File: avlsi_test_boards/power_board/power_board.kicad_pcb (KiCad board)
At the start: 4 copper layers, 116 parts, among them J1 PJ-102AH, J2 PJ-102AH, J3 Conn_02x06_Top_Bottom, J4 Conn_02x06_Top_Bottom, J5 Conn_02x20_Odd_Even, J6 Conn_02x20_Odd_Even, J7 Conn_02x20_Odd_Even, J8 Conn_02x20_Odd_Even, U1 TLV1117LV18DCYR, U11 SN74LVC16T245DLR, U12 SN74LVC16T245DLR, U13 SN74LVC16T245DLR, U14 SN74LVC16T245DLR, U15 DS04-254-2-04BK-SMT, U17 SN74LVC16T245DLR, U18 SN74LVC16T245DLR, U19 SN74LVC16T245DLR, U20 74HC4051D_653, U3 TLV1117LV25DCYR, U4 TLV1117LV33DCYR, U5 TLV1117LV18DCYR, U6 TLV75709PDBV, U7 TLV1117LV25DCYR, U8 TLV1117LV33DCYR

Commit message: Fully routed
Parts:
- removed the C1 at (90.5, 48.5)
- removed the C1 at (81.5, 27.0)
- removed the C1 at (72.0, 49.8)
- removed the C10 at (43.0, 66.3)
- removed the C12 at (31.8, 41.5)
- removed the C17 at (81.5, 34.5)
- removed the C17 at (90.5, 53.5)
- removed the C17 at (43.5, 56.2)
- removed the C18 at (81.5, 37.0)
- removed the C18 at (90.5, 56.0)
- removed the C18 at (78.5, 62.5)
- removed the C2 at (81.5, 29.5)
- removed the C2 at (90.5, 51.0)
- removed the C2 at (35.5, 49.0)
- removed the C38 at (51.0, 78.9)
- removed the C38 at (23.5, 51.2)
- removed the C39 at (55.0, 63.8)
- removed the C39 at (23.5, 53.7)
- removed the C6 at (52.1, 55.0)
- removed the C6 at (51.9, 41.5)
- removed the C7 at (81.5, 32.0)
- removed the C7 at (61.0, 63.8)
- removed the C9 at (43.0, 63.8)
- removed J4: Conn_02x06_Top_Bottom, Connector_PinHeader_2.54mm:PinHeader_2x06_P2.54mm_Vertical
- added C1: 1u, Capacitor_SMD:C_0603_1608Metric, B.Cu at (151.9, 58.8)
- added C17: 1u, Capacitor_SMD:C_0603_1608Metric, B.Cu at (169.6, 46.3)
- added C18: 1u, Capacitor_SMD:C_0603_1608Metric, B.Cu at (169.5, 59.0)
- added C2: 1u, Capacitor_SMD:C_0603_1608Metric, B.Cu at (151.8, 53.8)
- added C38: 1u, Capacitor_SMD:C_0603_1608Metric, B.Cu at (156.6, 101.9)
- added C39: 1u, Capacitor_SMD:C_0603_1608Metric, B.Cu at (121.6, 103.5)
- added C6: 1u, Capacitor_SMD:C_0603_1608Metric, B.Cu at (109.3, 103.4)
- added C7: 1u, Capacitor_SMD:C_0603_1608Metric, B.Cu at (179.0, 52.3)
- added J9: Conn_02x07_Top_Bottom, Connector_PinHeader_2.00mm:PinHeader_2x07_P2.00mm_Vertical, F.Cu at (188.7, 35.8)
- added REF**: MountingHole_3.7mm, MountingHole:MountingHole_3.7mm, F.Cu at (195.4, 36.4)
- added REF**: MountingHole_3.7mm, MountingHole:MountingHole_3.7mm, F.Cu at (195.4, 128.2)
- added REF**: MountingHole_3.7mm, MountingHole:MountingHole_3.7mm, F.Cu at (103.6, 36.4)
- added REF**: MountingHole_3.7mm, MountingHole:MountingHole_3.7mm, F.Cu at (103.6, 128.1)
- C11, C12, C13, C15, C16, C19, C20, C22, C23, C24, C25, C26, C27, C28, C29, C30, C31, C32, C33, C34, C35, C36, C37, C4, C40, C41, C42, C43, C44, C47, C48, C51, C52: moved to B.Cu
- J3: value Conn_02x06_Top_Bottom -> Conn_02x07_Top_Bottom; footprint Connector_PinHeader_2.54mm:PinHeader_2x06_P2.54mm_Vertical -> Connector_PinHeader_2.00mm:PinHeader_2x07_P2.00mm_Vertical
- S5: moved to F.Cu
- moved C5 161.4 mm to (187.9, 46.4), turned to 90 degrees
- moved C20 147.2 mm to (190.1, 103.1), turned to 90 degrees
- moved C28 146.2 mm to (190.1, 111.1), turned to -90 degrees
- moved R11 145.0 mm to (190.4, 87.4), turned to 90 degrees
- moved R5 144.7 mm to (190.5, 79.1), turned to 90 degrees
- moved C44 142.2 mm to (190.1, 118.2), turned to -90 degrees
- moved C30 141.0 mm to (190.1, 94.3), turned to -90 degrees
- moved C13 137.5 mm to (177.7, 101.4), turned to -90 degrees
- moved C12 137.0 mm to (177.7, 96.2), turned to 90 degrees
- moved C29 133.6 mm to (177.7, 111.2), turned to -90 degrees
- moved C43 132.0 mm to (177.7, 120.0), turned to 90 degrees
- moved C10 131.1 mm to (156.5, 71.6), turned to -90 degrees
- moved R13 127.3 mm to (175.0, 79.3), turned to 90 degrees
- moved C45 127.3 mm to (143.9, 71.7), turned to -90 degrees
- moved R1 122.8 mm to (174.8, 70.9), turned to -90 degrees
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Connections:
- C10 pad 1: /pin_header/GND -> DGND
- C11 pad 1: /pin_header/GND -> DGND
- C12 pad 1: /pin_header/GND -> DGND
- C13 pad 1: /pin_header/GND -> DGND
- C14 pad 1: /pin_header/GND -> DGND
- C15 pad 1: /pin_header/GND -> DGND
- C16 pad 1: /pin_header/GND -> DGND
- C19 pad 1: /pin_header/GND -> DGND
- C20 pad 1: /pin_header/GND -> DGND
- C21 pad 2: /digital_power_converters/GND -> DGND
- C22 pad 2: /digital_power_converters/GND -> DGND
- C23 pad 1: /pin_header/GND -> DGND
- C24 pad 1: /pin_header/GND -> DGND
- C25 pad 1: /pin_header/GND -> DGND
- C26 pad 1: /pin_header/GND -> DGND
- C27 pad 1: /pin_header/GND -> DGND
- C28 pad 1: /pin_header/GND -> DGND
- C29 pad 1: /pin_header/GND -> DGND
- C3 pad 2: /digital_power_converters/GND -> DGND
- C30 pad 1: /pin_header/GND -> DGND
- C31 pad 1: /AVIN -> /AVIN5
- C31 pad 2: /AGND -> ADGND
- C32 pad 1: /AVIN -> /AVIN5
- C32 pad 2: /AGND -> ADGND
- C33 pad 2: /AGND -> ADGND
- C34 pad 2: /AGND -> ADGND
- C35 pad 1: /pin_header/GND -> DGND
- C36 pad 1: /pin_header/GND -> DGND
- C37 pad 1: /AVIN -> /AVIN5
- C37 pad 2: /AGND -> ADGND
- C4 pad 2: /digital_power_converters/GND -> DGND
- C40 pad 1: /pin_header/GND -> DGND
- C41 pad 1: /pin_header/GND -> DGND
- C42 pad 2: /AGND -> ADGND
- C43 pad 1: /pin_header/GND -> DGND
- C44 pad 1: /pin_header/GND -> DGND
- C45 pad 1: /pin_header/GND -> DGND
- C47 pad 1: /AVIN -> /AVIN5
- C47 pad 2: /AGND -> ADGND
- C48 pad 1: /AVIN -> /AVIN5
- C48 pad 2: /AGND -> ADGND
- C5 pad 1: /digital_power_converters/GND -> DGND
- C5 pad 2: /digital_power_converters/VIN -> DVIN5
- C51 pad 2: /AGND -> ADGND
- C52 pad 2: /AGND -> ADGND
- C8 pad 2: /digital_power_converters/GND -> DGND
- C9 pad 1: /pin_header/GND -> DGND
- J1 pad 1: /DVIN -> DVIN5
- J1 pad 2: /DGND -> DGND
- J1 pad 3: /DGND -> DGND
- J2 pad 1: /AVIN -> /AVIN5
- J2 pad 2: /AGND -> ADGND
- J2 pad 3: /AGND -> ADGND
- J3 pad 1: /DVIN -> ADGND
- J3 pad 10: /DGND -> /VCCA12
- J3 pad 11: /VCCD12 -> ADGND
- J3 pad 12: /DGND -> /VCCA09
- J3 pad 2: /DGND -> /AVIN5
- J3 pad 3: /VCCD18 -> ADGND
- J3 pad 4: /DGND -> /VCCA33
- J3 pad 5: /VCCD09 -> ADGND
- J3 pad 6: /DGND -> /VCCA25
- J3 pad 7: /VCCD33 -> ADGND
- J3 pad 8: /DGND -> /VCCA18
- J3 pad 9: /VCCD25 -> ADGND
- J5 pad 1: /pin_header/DGND -> DGND
- J5 pad 10: /pin_header/DGND -> DGND
- J5 pad 16: /pin_header/DGND -> DGND
- J5 pad 19: /pin_header/DGND -> DGND
- J5 pad 2: /pin_header/DGND -> DGND
- J5 pad 20: /pin_header/DGND -> DGND
- J5 pad 21: /pin_header/HA15 -> /pin_header/HA16
- J5 pad 22: /pin_header/HA16 -> /pin_header/HA15
- J5 pad 23: /pin_header/HA13 -> /pin_header/HA14
- J5 pad 24: /pin_header/HA14 -> /pin_header/HA13
- J5 pad 25: /pin_header/HA11 -> /pin_header/HA12
- J5 pad 26: /pin_header/HA12 -> /pin_header/HA11
- J5 pad 27: /pin_header/HA9 -> /pin_header/HA10
- J5 pad 28: /pin_header/HA10 -> /pin_header/HA9
- J5 pad 29: /pin_header/HA7 -> /pin_header/HA8
- J5 pad 30: /pin_header/HA8 -> /pin_header/HA7
- J5 pad 31: /pin_header/HA5 -> /pin_header/HA6
- J5 pad 32: /pin_header/HA6 -> /pin_header/HA5
- J5 pad 33: /pin_header/HA3 -> /pin_header/HA4
- J5 pad 34: /pin_header/HA4 -> /pin_header/HA3
- J5 pad 35: /pin_header/HA1 -> /pin_header/HA2
- J5 pad 36: /pin_header/HA2 -> /pin_header/HA1
- J5 pad 37: /pin_header/OPF1 -> /pin_header/OPH1
- J5 pad 38: /pin_header/OPH1 -> /pin_header/OPF1
- J5 pad 39: /pin_header/OPH2 -> /pin_header/OPH3
- J5 pad 40: /pin_header/OPH3 -> /pin_header/OPH2
- J6 pad 1: /pin_header/HB7 -> /pin_header/HB8
- J6 pad 2: /pin_header/HB8 -> /pin_header/HB7
- J6 pad 3: /pin_header/HB5 -> /pin_header/HB6
- J6 pad 4: /pin_header/HB6 -> /pin_header/HB5
- J6 pad 5: /pin_header/HB3 -> /pin_header/HB4
- J6 pad 6: /pin_header/HB4 -> /pin_header/HB3
- J6 pad 7: /pin_header/HB1 -> /pin_header/HB2
- J6 pad 8: /pin_header/HB2 -> /pin_header/HB1
- J7 pad 21: /pin_header/DGND -> DGND
- J7 pad 22: /pin_header/DGND -> DGND
- J7 pad 23: /pin_header/DGND -> DGND
- J7 pad 24: /pin_header/DGND -> DGND
- J7 pad 26: /pin_header/DGND -> DGND
- J7 pad 29: /pin_header/DGND -> DGND
- J7 pad 35: /pin_header/DGND -> DGND
- J8 pad 3: /pin_header/HB11 -> /pin_header/HB12
- J8 pad 4: /pin_header/HB12 -> /pin_header/HB11
- J8 pad 5: /pin_header/HB13 -> /pin_header/HB14
- J8 pad 6: /pin_header/HB14 -> /pin_header/HB13
- J8 pad 7: /pin_header/HB15 -> /pin_header/HB16
- J8 pad 8: /pin_header/HB16 -> /pin_header/HB15
- R1 pad 2: /pin_header/GND -> DGND
- R10 pad 2: /pin_header/GND -> DGND
- R11 pad 2: /pin_header/GND -> DGND
- R12 pad 2: /pin_header/GND -> DGND
- R13 pad 2: /pin_header/GND -> DGND
- R14 pad 2: /pin_header/GND -> DGND
- R15 pad 1: /digital_power_converters/GND -> DGND
- R16 pad 1: /digital_power_converters/GND -> DGND
- R17 pad 1: /digital_power_converters/GND -> DGND
- R2 pad 2: /pin_header/GND -> DGND
- R3 pad 2: /pin_header/GND -> DGND
- R4 pad 1: unconnected-(R4-Pad1) -> /pin_header/DIR1_6
- R4 pad 2: /pin_header/GND -> DGND
- R5 pad 2: /pin_header/GND -> DGND
- R6 pad 2: /pin_header/GND -> DGND
- R7 pad 2: /pin_header/GND -> DGND
- R8 pad 2: /pin_header/GND -> DGND
- R9 pad 2: /pin_header/GND -> DGND
- S1 pad A2: /pin_header/VIN -> V_Level_Shift
- S1 pad B2: /pin_header/VIN -> V_Level_Shift
- S2 pad A2: /pin_header/VIN -> V_Level_Shift
- S2 pad B2: /pin_header/VIN -> V_Level_Shift
- S3 pad A2: /pin_header/VIN -> V_Level_Shift
- S3 pad B2: /pin_header/VIN -> V_Level_Shift
- S4 pad A2: /pin_header/VIN -> V_Level_Shift
- S4 pad B2: /pin_header/VIN -> V_Level_Shift
- S5 pad A2: /pin_header/VIN -> V_Level_Shift
- S5 pad B2: /pin_header/VIN -> V_Level_Shift
- S6 pad A2: /pin_header/VIN -> V_Level_Shift
- S6 pad B2: /pin_header/VIN -> V_Level_Shift
- S7 pad A2: /pin_header/VIN -> V_Level_Shift
- S7 pad B2: /pin_header/VIN -> V_Level_Shift
- U1 pad 1: /digital_power_converters/GND -> DGND
- U1 pad 3: /digital_power_converters/VIN -> DVIN5
- U11 pad 10: /pin_header/GND -> DGND
- U11 pad 15: /pin_header/GND -> DGND
- U11 pad 21: /pin_header/GND -> DGND
- U11 pad 28: /pin_header/GND -> DGND
- U11 pad 34: /pin_header/GND -> DGND
- U11 pad 39: /pin_header/GND -> DGND
- U11 pad 4: /pin_header/GND -> DGND
- U11 pad 45: /pin_header/GND -> DGND
- U12 pad 10: /pin_header/GND -> DGND
- U12 pad 15: /pin_header/GND -> DGND
- U12 pad 21: /pin_header/GND -> DGND
- U12 pad 28: /pin_header/GND -> DGND
- U12 pad 34: /pin_header/GND -> DGND
- U12 pad 39: /pin_header/GND -> DGND
- U12 pad 4: /pin_header/GND -> DGND
- U12 pad 45: /pin_header/GND -> DGND
- U13 pad 10: /pin_header/GND -> DGND
- U13 pad 15: /pin_header/GND -> DGND
- U13 pad 21: /pin_header/GND -> DGND
- U13 pad 28: /pin_header/GND -> DGND
- U13 pad 34: /pin_header/GND -> DGND
- U13 pad 39: /pin_header/GND -> DGND
- U13 pad 4: /pin_header/GND -> DGND
- U13 pad 45: /pin_header/GND -> DGND
- U14 pad 10: unconnected-(U14-GND-Pad10) -> DGND
- U14 pad 15: /pin_header/GND -> DGND
- U14 pad 21: /pin_header/GND -> DGND
- U14 pad 28: /pin_header/GND -> DGND
- U14 pad 34: /pin_header/GND -> DGND
- U14 pad 39: /pin_header/GND -> DGND
- U14 pad 4: /pin_header/GND -> DGND
- U14 pad 45: /pin_header/GND -> DGND
- U15 pad 1: /digital_power_converters/VIN -> DVIN5
- U15 pad 2: /digital_power_converters/VIN -> DVIN5
- U15 pad 3: /digital_power_converters/VIN -> DVIN5
- U15 pad 4: /digital_power_converters/VIN -> DVIN5
- U17 pad 10: unconnected-(U17-GND-Pad10) -> DGND
- U17 pad 15: /pin_header/GND -> DGND
- U17 pad 21: /pin_header/GND -> DGND
- U17 pad 28: /pin_header/GND -> DGND
- U17 pad 34: /pin_header/GND -> DGND
- U17 pad 39: /pin_header/HC6 -> DGND
- U17 pad 4: /pin_header/GND -> DGND
- U17 pad 40: /pin_header/GND -> /pin_header/HC6
- U17 pad 45: /pin_header/GND -> DGND
- U18 pad 10: /pin_header/GND -> DGND
- U18 pad 15: /pin_header/GND -> DGND
- U18 pad 21: /pin_header/GND -> DGND
- U18 pad 28: /pin_header/GND -> DGND
- U18 pad 34: /pin_header/GND -> DGND
- U18 pad 39: /pin_header/GND -> DGND
- U18 pad 4: /pin_header/GND -> DGND
- U18 pad 45: /pin_header/GND -> DGND
- U19 pad 10: /pin_header/GND -> DGND
- U19 pad 15: /pin_header/GND -> DGND
- U19 pad 21: /pin_header/GND -> DGND
- U19 pad 28: /pin_header/GND -> DGND
- U19 pad 34: /pin_header/GND -> DGND
- U19 pad 39: /pin_header/GND -> DGND
- U19 pad 4: /pin_header/GND -> DGND
- U19 pad 45: /pin_header/GND -> DGND
- U2 pad 02: /pin_header/DGND -> DGND
- U2 pad 116: /pin_header/DGND -> DGND
- U2 pad 136: /pin_header/DGND -> DGND
- U2 pad 14: /pin_header/DGND -> DGND
- U2 pad 158: /pin_header/DGND -> DGND
- U2 pad 160: /pin_header/DGND -> DGND
- U2 pad 35: /pin_header/DGND -> DGND
- U2 pad 55: /pin_header/DGND -> DGND
- U2 pad 78: /pin_header/DGND -> DGND
- U2 pad 80: /pin_header/DGND -> DGND
- U2 pad 81: /pin_header/DGND -> DGND
- U2 pad 93: /pin_header/DGND -> DGND
- U2 pad 94: /pin_header/DGND -> DGND
- U20 pad 16: /digital_power_converters/VIN -> DVIN5
- U20 pad 5: /digital_power_converters/AVIN -> VDCustom
- U20 pad 6: /digital_power_converters/VIN -> DVIN5
- U20 pad 7: /digital_power_converters/GND -> DGND
- U20 pad 8: /digital_power_converters/GND -> DGND
- U3 pad 1: /digital_power_converters/GND -> DGND
- U3 pad 3: /digital_power_converters/VIN -> DVIN5
- U4 pad 1: /digital_power_converters/GND -> DGND
- U4 pad 3: /digital_power_converters/VIN -> DVIN5
- U5 pad 1: /AGND -> ADGND
- U5 pad 3: /AVIN -> /AVIN5
- U6 pad 1: /AVIN -> /AVIN5
- U6 pad 2: /AGND -> ADGND
- U6 pad 3: /AVIN -> /AVIN5
- U7 pad 1: /AGND -> ADGND
- U7 pad 3: /AVIN -> /AVIN5
- U8 pad 1: /AGND -> ADGND
- U8 pad 3: /AVIN -> /AVIN5
- VR1 pad 1: /digital_power_converters/GND -> DGND
- VR1 pad 3: /digital_power_converters/VIN -> DVIN5
- VR2 pad 1: /AGND -> ADGND
- VR2 pad 3: /AVIN -> /AVIN5
- VR3 pad 1: /digital_power_converters/GND -> DGND
- VR3 pad 3: /digital_power_converters/VIN -> DVIN5
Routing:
- net DGND: track 0.00 -> 1122.4 mm, vias 0 -> 66
- net /pin_header/DGND: track 892.1 -> 0.00 mm
- net DVIN5: track 0.00 -> 127.1 mm, vias 0 -> 8
- net V_Level_Shift: track 392.2 -> 508.6 mm, vias 15 -> 54
- net /AVIN5: track 0.00 -> 98.0 mm, vias 0 -> 8
- net /pin_header/HB9: track 2.17 -> 71.2 mm
- net /AVIN: track 58.3 -> 0.00 mm, vias 1 -> 0
- net VDCustom: track 0.00 -> 49.6 mm, vias 0 -> 1
- net /pin_header/DIR2_0: track 93.4 -> 46.1 mm
- net /pin_header/DIR1_0: track 66.4 -> 25.2 mm, vias 4 -> 2
- net /VCCA25: track 52.5 -> 20.8 mm, vias 2 -> 1
- net /pin_header/DIR1_2: track 44.0 -> 19.2 mm, vias 2 -> 0
- net /VCCA18: track 39.9 -> 17.0 mm, vias 0 -> 1
- net /pin_header/DIR2_6: track 61.2 -> 38.8 mm, vias 4 -> 2
- net /pin_header/DIR1_4: track 46.3 -> 25.7 mm
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- added copper zone on B.Cu, net ADGND
- added copper zone on F.Cu, net ADGND
- added copper zone on B.Cu, net DGND
- added copper zone on F.Cu, net DGND
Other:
- board text added: "10VDD"
- board text added: "18VDD"
- board text added: "3VDD"
- board text added: "AGND"
- board text added: "AVIN5"
- board text added: "DGND"
- board text added: "Digital I/O"
- board text added: "FPGA_TCK"
- board text added: "FPGA_TDI"
- board text added: "FPGA_TDO"
- board text added: "FPGA_TMS"
- board text added: "Groudning pull up resistors near switches?"
- board text added: "Maybe the unfilled zone on the back is okay bevause its connected to ground through the back?"
- board text added: "NULL"
- board text added: "SYS_CLK_MC1"
- board text added: "SYS_CLK_MC2"
- board text added: "VACUSTOM"
- board text added: "VCCA09"
- board text added: "VCCA12"
- board text added: "VCCA18"
- board text added: "VCCA25"
- board text added: "VCCA33"
- board text added: "VCCBATT"
- board text added: "VCCO_MC1"
- board text added: "VCCO_MC2"
- board text added: "VDCIN"
- board text added: "XADC_VIN"
- board text added: "XADC_VP"

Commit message: more changes
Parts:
- removed J7: Conn_02x20_Odd_Even, Connector_PinHeader_2.00mm:PinHeader_2x20_P2.00mm_Vertical
- removed R4: 4.7k, Resistor_SMD:R_0201_0603Metric
- added J4: Conn_02x10_Odd_Even, Connector_PinHeader_2.00mm:PinHeader_2x10_P2.00mm_Vertical, F.Cu at (103.4, 63.1)
- moved C42 0.98 mm to (122.7, 55.5)
- moved U15 0.36 mm to (150.1, 38.5)
- moved R1 0.22 mm to (175.1, 70.9)
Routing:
- net DGND: track 1122.4 -> 1233.2 mm, vias 66 -> 123
- net /pin_header/VCCO_MC2: track 76.6 -> 87.7 mm
- net /pin_header/VCCO_MC1: track 120.8 -> 131.8 mm
- net DVIN5: track 127.1 -> 133.2 mm
- net /digital_power_converters/NULL: track 0.00 -> 5.35 mm
- net ADGND: track 12.2 -> 16.0 mm, vias 10 -> 11
- net /pin_header/VDCIN: track 161.9 -> 164.7 mm
- net /VCCA09: track 23.2 -> 25.1 mm
- net /pin_header/33VDD: track 194.9 -> 196.6 mm
- net /pin_header/3VDD: track 150.9 -> 152.5 mm
- net /pin_header/10VDD: track 95.9 -> 96.7 mm
- net /pin_header/HB8: track 45.4 -> 46.2 mm
- net /pin_header/SYS_CLK_MC2: track 27.8 -> 28.6 mm
- net /pin_header/HA2: track 40.8 -> 41.3 mm
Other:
- board outline added: 100 x 100 mm
- board text added: "LS1"
- board text added: "LS2"
- board text added: "LS3"
- board text added: "LS4"
- board text added: "LS5"
- board text added: "LS6"
- board text added: "LS7"
- board text added: "VA09"
- board text added: "VA12"
- board text added: "VA18"
- board text added: "VA27"
- board text added: "VA33"
- board text added: "VA50"
- board text added: "VCUST"
- board text added: "VD09"
- board text added: "VD12"
- board text added: "VD18"
- board text added: "VD27"
- board text added: "VD33"
- board text added: "VD50"
- board text removed: "10VDD"
- board text removed: "18VDD"
- board text removed: "3VDD"
- board text removed: "AVIN5"
- board text removed: "Digital I/O"
- board text removed: "FPGA_TCK"
- board text removed: "FPGA_TDI"
- board text removed: "FPGA_TDO"
- board text removed: "FPGA_TMS"
- board text removed: "NULL"
- board text removed: "SYS_CLK_MC1"
- board text removed: "SYS_CLK_MC2"
- board text removed: "VACUSTOM"
- board text removed: "VCCA09"
- board text removed: "VCCA12"
- board text removed: "VCCA18"
- board text removed: "VCCA25"
- board text removed: "VCCA33"
- board text removed: "VCCBATT"
- board text removed: "VCCO_MC1"
- board text removed: "VCCO_MC2"
- board text removed: "VDCIN"
- board text removed: "XADC_VIN"
- board text removed: "XADC_VP"

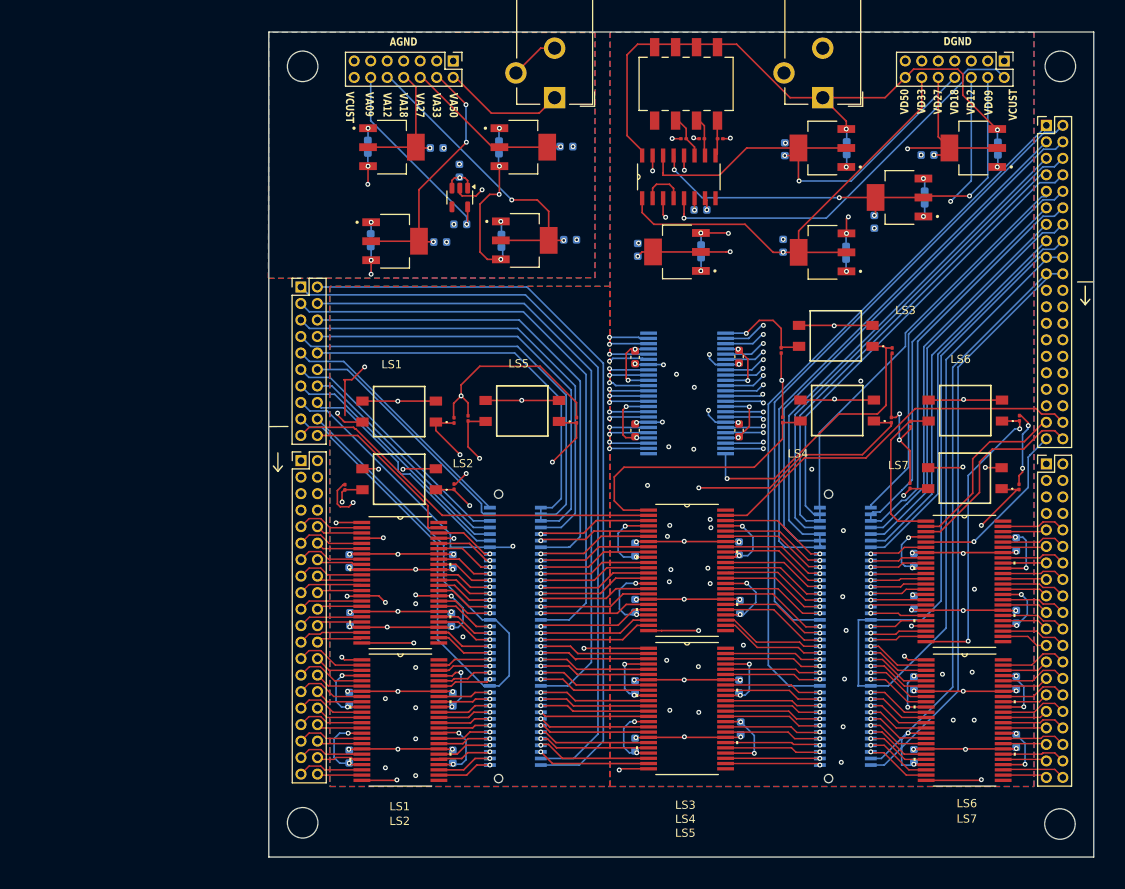
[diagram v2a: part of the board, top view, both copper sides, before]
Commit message: Add updated schematic
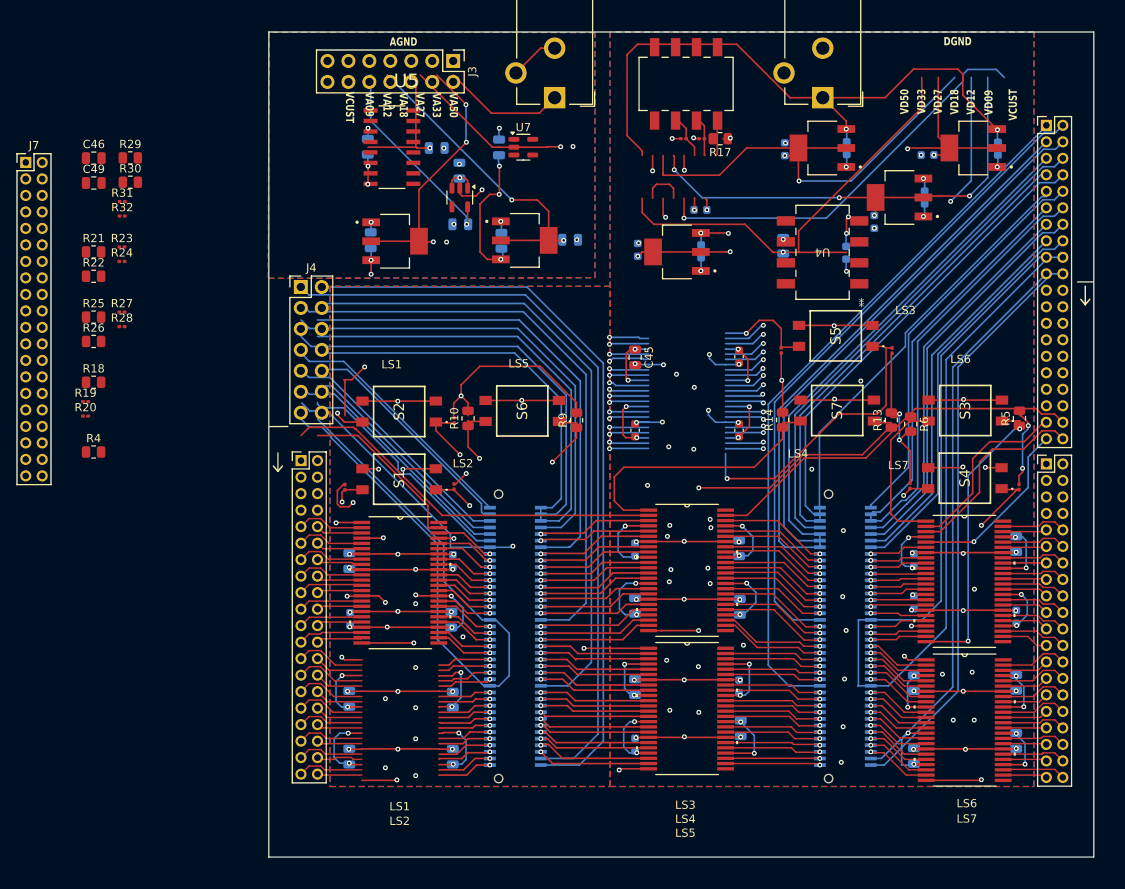
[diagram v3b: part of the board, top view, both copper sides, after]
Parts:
- removed C51, C52: 1u, Capacitor_SMD:C_0603_1608Metric
- removed J9: Conn_02x07_Top_Bottom, Connector_PinHeader_2.00mm:PinHeader_2x07_P2.00mm_Vertical
- removed REF** (x4): MountingHole_3.7mm, MountingHole:MountingHole_3.7mm
- removed U18, U19: SN74LVC16T245DLR, avlsi:DL48
- removed U20: 74HC4051D_653, 74HC4051D_653:SOIC127P600X175-16N
- added C46: 1u, Capacitor_SMD:C_0805_2012Metric, F.Cu at (78.3, 47.5)
- added C49: 0.1u, Capacitor_SMD:C_0805_2012Metric, F.Cu at (78.3, 50.5)
- added J7: Conn_02x20_Odd_Even, Connector_PinHeader_2.00mm:PinHeader_2x20_P2.00mm_Vertical, F.Cu at (70.0, 48.0)
- added R18: 10k, Resistor_SMD:R_0805_2012Metric, F.Cu at (78.3, 74.7)
- added R19: 4.7k, Resistor_SMD:R_0201_0603Metric, F.Cu at (77.3, 77.0)
- added R20: 4.7k, Resistor_SMD:R_0201_0603Metric, F.Cu at (77.3, 78.8)
- added R21: 10k, Resistor_SMD:R_0805_2012Metric, F.Cu at (78.3, 58.9)
- added R22: 10k, Resistor_SMD:R_0805_2012Metric, F.Cu at (78.3, 61.9)
- added R23: 4.7k, Resistor_SMD:R_0201_0603Metric, F.Cu at (81.7, 58.3)
- added R24: 4.7k, Resistor_SMD:R_0201_0603Metric, F.Cu at (81.7, 60.0)
- added R25: 10k, Resistor_SMD:R_0805_2012Metric, F.Cu at (78.3, 66.8)
- added R26: 10k, Resistor_SMD:R_0805_2012Metric, F.Cu at (78.3, 69.8)
- added R27: 4.7k, Resistor_SMD:R_0201_0603Metric, F.Cu at (81.7, 66.2)
- added R28: 4.7k, Resistor_SMD:R_0201_0603Metric, F.Cu at (81.7, 68.0)
- added R29: 10k, Resistor_SMD:R_0805_2012Metric, F.Cu at (82.7, 47.5)
- added R30: 10k, Resistor_SMD:R_0805_2012Metric, F.Cu at (82.7, 50.5)
- added R31: 4.7k, Resistor_SMD:R_0201_0603Metric, F.Cu at (81.7, 52.8)
- added R32: 4.7k, Resistor_SMD:R_0201_0603Metric, F.Cu at (81.7, 54.5)
- added R4: 0, Resistor_SMD:R_0805_2012Metric, F.Cu at (78.3, 83.2)
- C22, C24, C26, C28, C30, C32, C34, C36, C38, C40, C42, C44, C48: footprint Capacitor_SMD:C_0603_1608Metric -> Capacitor_SMD:C_0805_2012Metric
- C23, C25, C27, C29, C31, C33, C35, C37, C39, C41, C43, C45, C47: value 1u -> 0.1u; footprint Capacitor_SMD:C_0603_1608Metric -> Capacitor_SMD:C_0805_2012Metric
- J3: value Conn_02x07_Top_Bottom -> Conn_02x07_Odd_Even; footprint Connector_PinHeader_2.00mm:PinHeader_2x07_P2.00mm_Vertical -> Connector_PinHeader_2.54mm:PinHeader_2x07_P2.54mm_Vertical
- J4: value Conn_02x10_Odd_Even -> Conn_02x07_Odd_Even; footprint Connector_PinHeader_2.00mm:PinHeader_2x10_P2.00mm_Vertical -> Connector_PinHeader_2.54mm:PinHeader_2x07_P2.54mm_Vertical
- R10, R13, R14, R17, R5, R6, R9: value 4.7k -> 10k; footprint Resistor_SMD:R_0201_0603Metric -> Resistor_SMD:R_0805_2012Metric
- U4: value TLV1117LV33DCYR -> DS04-254-2-04BK-SMT; footprint avlsi:VREG_TLV1117LV33DCYR -> ds:DS04-254-2-04BK-SMT_CUD
- U5: value TLV1117LV18DCYR -> 74HC4051D_653; footprint avlsi:SOT230P700X180-4N -> 74HC4051D_653:SOIC127P600X175-16N
- U7: value TLV1117LV25DCYR -> TLV75709PDBV; footprint avlsi:SOT230P700X180-4N -> Package_TO_SOT_SMD:SOT-23-5
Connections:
- C10 pad 1: DGND -> VCCD12
- C10 pad 2: V_Level_Shift -> DGND
- C11 pad 2: V_Level_Shift -> DVIN5
- C12 pad 1: DGND -> /AVIN5
- C12 pad 2: V_Level_Shift -> ADGND
- C13 pad 1: DGND -> /AVIN5
- C13 pad 2: V_Level_Shift -> ADGND
- C14 pad 1: DGND -> /VCCA18
- C14 pad 2: V_Level_Shift -> ADGND
- C15 pad 1: DGND -> /VCCA12
- C15 pad 2: V_Level_Shift -> ADGND
- C16 pad 1: DGND -> /AVIN5
- C16 pad 2: V_Level_Shift -> ADGND
- C17 pad 1: DVIN5 -> /VCCA09
- C17 pad 2: DGND -> ADGND
- C18 pad 1: DVIN5 -> /AVIN5
- C18 pad 2: DGND -> ADGND
- C19 pad 1: DGND -> /AVIN5
- C19 pad 2: V_Level_Shift -> ADGND
- C20 pad 1: DGND -> /VCCA25
- C20 pad 2: V_Level_Shift -> ADGND
- C21 pad 1: /VCCD25 -> /VCCA33
- C21 pad 2: DGND -> ADGND
- C22 pad 1: /VCCD33 -> VCCD33
- C23 pad 1: DGND -> VCCD33
- C23 pad 2: V_Level_Shift -> DGND
- C24 pad 1: DGND -> V_Level_Shift
- C24 pad 2: V_Level_Shift -> DGND
- C25 pad 1: DGND -> V_Level_Shift
- C25 pad 2: V_Level_Shift -> DGND
- C26 pad 1: DGND -> VCCD33
- C26 pad 2: V_Level_Shift -> DGND
- C27 pad 1: DGND -> VCCD33
- C27 pad 2: V_Level_Shift -> DGND
- C28 pad 1: DGND -> V_Level_Shift
- C28 pad 2: V_Level_Shift -> DGND
- C29 pad 1: DGND -> V_Level_Shift
- C29 pad 2: V_Level_Shift -> DGND
- C3 pad 1: /VCCD18 -> DVIN5
- C30 pad 1: DGND -> VCCD33
- C30 pad 2: V_Level_Shift -> DGND
- C31 pad 1: /AVIN5 -> VCCD33
- C31 pad 2: ADGND -> DGND
- C32 pad 1: /AVIN5 -> V_Level_Shift
- C32 pad 2: ADGND -> DGND
- C33 pad 1: /VCCA18 -> V_Level_Shift
- C33 pad 2: ADGND -> DGND
- C34 pad 1: /VCCA12 -> VCCD33
- C34 pad 2: ADGND -> DGND
- C35 pad 1: DGND -> VCCD33
- C35 pad 2: V_Level_Shift -> DGND
- C36 pad 1: DGND -> V_Level_Shift
- C36 pad 2: V_Level_Shift -> DGND
- C37 pad 1: /AVIN5 -> V_Level_Shift
- C37 pad 2: ADGND -> DGND
- C38 pad 1: DGND -> VCCD33
- C38 pad 2: V_Level_Shift -> DGND
- C39 pad 1: DGND -> VCCD33
- C39 pad 2: V_Level_Shift -> DGND
- C4 pad 1: /VCCD12 -> DVIN5
- C40 pad 1: DGND -> V_Level_Shift
- C40 pad 2: V_Level_Shift -> DGND
- C41 pad 1: DGND -> V_Level_Shift
- C41 pad 2: V_Level_Shift -> DGND
- C42 pad 1: /VCCA09 -> VCCD33
- C42 pad 2: ADGND -> DGND
- C43 pad 1: DGND -> VCCD33
- C43 pad 2: V_Level_Shift -> DGND
- C44 pad 1: DGND -> V_Level_Shift
- C44 pad 2: V_Level_Shift -> DGND
- C45 pad 1: DGND -> V_Level_Shift
- C45 pad 2: V_Level_Shift -> DGND
- C47 pad 1: /AVIN5 -> VCCD33
- C47 pad 2: ADGND -> DGND
- C48 pad 1: /AVIN5 -> V_Level_Shift
- C48 pad 2: ADGND -> DGND
- C5 pad 1: DGND -> DVIN5
- C5 pad 2: DVIN5 -> DGND
- C6 pad 1: DGND -> VCCD18
- C6 pad 2: V_Level_Shift -> DGND
- C7 pad 1: DVIN5 -> VCCD25
- C8 pad 1: /VCCD09 -> VCCD33
- C9 pad 1: DGND -> VCCD09
- C9 pad 2: V_Level_Shift -> DGND
- J3 pad 1: ADGND -> /VACustom
- J3 pad 10: /VCCA12 -> ADGND
- J3 pad 11: ADGND -> /VCCA33
- J3 pad 12: /VCCA09 -> ADGND
- J3 pad 13: ADGND -> /AVIN5
- J3 pad 14: /VACustom -> ADGND
- J3 pad 2: /AVIN5 -> ADGND
- J3 pad 3: ADGND -> /VCCA09
- J3 pad 4: /VCCA33 -> ADGND
- J3 pad 5: ADGND -> /VCCA12
- J3 pad 6: /VCCA25 -> ADGND
- J3 pad 7: ADGND -> /VCCA18
- J3 pad 8: /VCCA18 -> ADGND
- J3 pad 9: ADGND -> /VCCA25
- J4 pad 1: DGND -> VDCustom
- J4 pad 10: /pin_header/3VDD -> DGND
- J4 pad 11: /pin_header/FPGA_TCK -> VCCD33
- J4 pad 12: /pin_header/VCCBATT -> DGND
- J4 pad 13: /pin_header/FPGA_TDI -> DVIN5
- J4 pad 14: /pin_header/FPGA_TMS -> DGND
- J4 pad 3: DGND -> VCCD09
- J4 pad 5: /pin_header/FPGA_TDO -> VCCD12
- J4 pad 7: /pin_header/3VDD -> VCCD18
- J4 pad 8: /pin_header/3VDD -> DGND
- J4 pad 9: DGND -> VCCD25
- J5 pad 1: DGND -> FPGA_33VDD
- J5 pad 10: DGND -> FPGA_TDI
- J5 pad 11: /pin_header/10VDD -> MC2_12
- J5 pad 12: /pin_header/10VDD -> SYS_CLK_MC2
- J5 pad 13: /pin_header/SYS_CKL_MC1 -> FPGA_GND
- J5 pad 14: /pin_header/XADC_VN -> FPGA_GND
- J5 pad 15: /pin_header/XADC_VP -> MC2_16
- J5 pad 16: DGND -> MC2_15_PIN
- J5 pad 17: /pin_header/VCCO_MC1 -> MC2_18
- J5 pad 18: /pin_header/VCCO_MC1 -> MC2_17_PIN
- J5 pad 19: DGND -> MC2_20
- J5 pad 2: DGND -> FPGA_GND
- J5 pad 20: DGND -> MC2_19_PIN
- J5 pad 21: /pin_header/HA16 -> MC2_22
- J5 pad 22: /pin_header/HA15 -> MC2_21_PIN
- J5 pad 23: /pin_header/HA14 -> MC2_24
- J5 pad 24: /pin_header/HA13 -> MC2_23_PIN
- J5 pad 25: /pin_header/HA12 -> MC2_26_PIN
- J5 pad 26: /pin_header/HA11 -> MC2_25_PIN
- J5 pad 27: /pin_header/HA10 -> MC2_28_PIN
- J5 pad 28: /pin_header/HA9 -> MC2_27_PIN
- J5 pad 29: /pin_header/HA8 -> MC2_30_PIN
- J5 pad 3: /pin_header/33VDD -> FPGA_33VDD
- J5 pad 30: /pin_header/HA7 -> MC2_29_PIN
- J5 pad 31: /pin_header/HA6 -> MC2_32_PIN
- J5 pad 32: /pin_header/HA5 -> MC2_31_PIN
- J5 pad 33: /pin_header/HA4 -> MC2_34_PIN
- J5 pad 34: /pin_header/HA3 -> MC2_33_PIN
- J5 pad 35: /pin_header/HA2 -> FPGA_GND
- J5 pad 36: /pin_header/HA1 -> FPGA_33VDD
- J5 pad 37: /pin_header/OPH1 -> MC2_38_PIN
- J5 pad 38: /pin_header/OPF1 -> MC2_37_PIN
- J5 pad 39: /pin_header/OPH3 -> MC2_40_PIN
- J5 pad 4: /pin_header/33VDD -> VCCBATT
- J5 pad 40: /pin_header/OPH2 -> MC2_39_PIN
- J5 pad 5: /pin_header/33VDD -> FPGA_33VDD
- J5 pad 6: /pin_header/18VDD -> FPGA_TCK
- J5 pad 7: /pin_header/VDCIN -> FPGA_TDO
- J5 pad 8: /pin_header/VDCIN -> FPGA_TMS
- J5 pad 9: /pin_header/VDCIN -> MC2_10_PIN
- J6 pad 1: /pin_header/HB8 -> MC2_42_PIN
- J6 pad 10: /pin_header/HF2 -> MC2_49_PIN
- J6 pad 11: /pin_header/HF3 -> MC2_52_PIN
- J6 pad 12: /pin_header/HF4 -> MC2_51_PIN
- J6 pad 13: /pin_header/HF5 -> MC2_54_PIN
- J6 pad 14: /pin_header/HF6 -> MC2_53_PIN
- J6 pad 15: /pin_header/HF7 -> FPGA_GND
- J6 pad 16: /pin_header/HF8 -> FPGA_33VDD
- J6 pad 17: /pin_header/HF9 -> MC2_58_PIN
- J6 pad 18: /pin_header/HF10 -> MC2_57_PIN
- J6 pad 19: /pin_header/HF11 -> MC2_60_PIN
- J6 pad 2: /pin_header/HB7 -> MC2_41_PIN
- J6 pad 20: /pin_header/HF12 -> MC2_59_PIN
- J6 pad 21: /pin_header/HF13 -> MC2_62_PIN
- J6 pad 22: /pin_header/HF14 -> MC2_61_PIN
- J6 pad 23: /pin_header/HF15 -> MC2_64_PIN
- J6 pad 24: /pin_header/HF16 -> MC2_63_PIN
- J6 pad 25: /pin_header/HE1 -> MC2_66_PIN
- J6 pad 26: /pin_header/HE2 -> MC2_65_PIN
- J6 pad 27: /pin_header/HE3 -> MC2_68_PIN
- J6 pad 28: /pin_header/HE4 -> MC2_67_PIN
- J6 pad 29: /pin_header/HE5 -> MC2_70_PIN
- J6 pad 3: /pin_header/HB6 -> MC2_44_PIN
- J6 pad 30: /pin_header/HE6 -> MC2_69_PIN
- J6 pad 31: /pin_header/HE7 -> MC2_72_PIN
- J6 pad 32: /pin_header/HE8 -> MC2_71_PIN
- J6 pad 33: /pin_header/HE9 -> MC2_74_PIN
- J6 pad 34: /pin_header/HE10 -> MC2_73_PIN
- J6 pad 35: /pin_header/HE11 -> MC2_76_PIN
- J6 pad 36: /pin_header/HE12 -> MC2_75_PIN
- J6 pad 37: /pin_header/HE13 -> FPGA_GND
- J6 pad 38: /pin_header/HE14 -> MC2_77_PIN
- J6 pad 39: /pin_header/HE15 -> FPGA_GND
- J6 pad 4: /pin_header/HB5 -> MC2_43_PIN
- J6 pad 40: /pin_header/HE16 -> MC2_79_PIN
- J6 pad 5: /pin_header/HB4 -> MC2_46_PIN
- J6 pad 6: /pin_header/HB3 -> MC2_45_PIN
- J6 pad 7: /pin_header/HB2 -> MC2_48_PIN
- J6 pad 8: /pin_header/HB1 -> MC2_47_PIN
- J6 pad 9: /pin_header/HF1 -> MC2_50_PIN
- J8 pad 1: /pin_header/HB10 -> MC1_42_PIN
- J8 pad 10: /pin_header/HC1 -> MC1_49_PIN
- J8 pad 11: /pin_header/HC4 -> MC1_52_PIN
- J8 pad 12: /pin_header/HC3 -> MC1_51_PIN
- J8 pad 13: /pin_header/HC6 -> MC1_54_PIN
- J8 pad 14: /pin_header/HC5 -> MC1_53_PIN
- J8 pad 15: /pin_header/HC8 -> FPGA_33VDD
- J8 pad 16: /pin_header/HC7 -> FPGA_GND
- J8 pad 17: /pin_header/HC10 -> MC1_58_PIN
- J8 pad 18: /pin_header/HC9 -> MC1_57_PIN
- J8 pad 19: /pin_header/HC12 -> MC1_60_PIN
- J8 pad 2: /pin_header/HB9 -> MC1_41_PIN
- J8 pad 20: /pin_header/HC11 -> MC1_59_PIN
- J8 pad 21: /pin_header/HC14 -> MC1_62_PIN
- J8 pad 22: /pin_header/HC13 -> MC1_61_PIN
- J8 pad 23: /pin_header/HC16 -> MC1_64_PIN
- J8 pad 24: /pin_header/HC15 -> MC1_63_PIN
- J8 pad 25: /pin_header/HD2 -> MC1_66_PIN
- J8 pad 26: /pin_header/HD1 -> MC1_65_PIN
- J8 pad 27: /pin_header/HD4 -> MC1_68_PIN
- J8 pad 28: /pin_header/HD3 -> MC1_67_PIN
- J8 pad 29: /pin_header/HD6 -> MC1_70_PIN
- J8 pad 3: /pin_header/HB12 -> MC1_44_PIN
- J8 pad 30: /pin_header/HD5 -> MC1_69_PIN
- J8 pad 31: /pin_header/HD8 -> MC1_72_PIN
- J8 pad 32: /pin_header/HD7 -> MC1_71_PIN
- J8 pad 33: /pin_header/HD10 -> MC1_74_PIN
- J8 pad 34: /pin_header/HD9 -> MC1_73
- J8 pad 35: /pin_header/HD12 -> MC1_76_PIN
- J8 pad 36: /pin_header/HD11 -> MC1_75
- J8 pad 37: /pin_header/HD14 -> FPGA_GND
- J8 pad 38: /pin_header/HD13 -> MC1_77
- J8 pad 39: /pin_header/HD16 -> FPGA_GND
- J8 pad 4: /pin_header/HB11 -> MC1_43_PIN
- J8 pad 40: /pin_header/HD15 -> MC1_79
- J8 pad 5: /pin_header/HB14 -> MC1_46_PIN
- J8 pad 6: /pin_header/HB13 -> MC1_45_PIN
- J8 pad 7: /pin_header/HB16 -> MC1_48_PIN
- J8 pad 8: /pin_header/HB15 -> MC1_47_PIN
- J8 pad 9: /pin_header/HC2 -> MC1_50_PIN
- R1 pad 1: /pin_header/DIR2_7 -> DGND
- R1 pad 2: DGND -> /digital_power_converters/S0
- R10 pad 1: /pin_header/DIR1_3 -> DGND
- R10 pad 2: DGND -> Net-(U12-*2OE)
- R11 pad 1: /pin_header/DIR2_4 -> /level_shifter1/DIR1
- R12 pad 1: /pin_header/DIR1_4 -> /level_shifter1/DIR2
- R13 pad 1: /pin_header/DIR2_5 -> DGND
- R13 pad 2: DGND -> Net-(U13-*1OE)
- R14 pad 1: /pin_header/DIR1_5 -> DGND
- R14 pad 2: DGND -> Net-(U13-*2OE)
- R15 pad 1: DGND -> /level_shifter2/DIR1
- R15 pad 2: /digital_power_converters/S0 -> DGND
- R16 pad 1: DGND -> /level_shifter2/DIR2
- R16 pad 2: /digital_power_converters/S1 -> DGND
- R17 pad 2: /digital_power_converters/S2 -> Net-(U14-*1OE)
- R2 pad 1: /pin_header/DIR1_7 -> DGND
- R2 pad 2: DGND -> /digital_power_converters/S1
- R3 pad 1: /pin_header/DIR2_6 -> DGND
- R3 pad 2: DGND -> /digital_power_converters/S2
- R5 pad 1: /pin_header/DIR2_2 -> DGND
- R5 pad 2: DGND -> Net-(U11-*1OE)
- R6 pad 1: /pin_header/DIR1_2 -> DGND
- R6 pad 2: DGND -> Net-(U11-*2OE)
- R7 pad 1: /pin_header/DIR2_0 -> /level_shifter/DIR1
- R8 pad 1: /pin_header/DIR1_0 -> /level_shifter/DIR2
- R9 pad 1: /pin_header/DIR2_3 -> DGND
- R9 pad 2: DGND -> Net-(U12-*1OE)
- S1 pad A1: /pin_header/DIR2_0 -> /level_shifter/DIR2
- S1 pad B1: /pin_header/DIR1_0 -> /level_shifter/DIR1
- S2 pad A1: /pin_header/DIR2_6 -> /level_shifter1/DIR2
- S2 pad B1: /pin_header/DIR1_6 -> /level_shifter1/DIR1
- S3 pad A1: /pin_header/DIR2_2 -> /level_shifter2/DIR2
- S3 pad B1: /pin_header/DIR1_2 -> /level_shifter2/DIR1
- S4 pad A1: /pin_header/DIR2_4 -> /level_shifter3/DIR2
- S4 pad B1: /pin_header/DIR1_4 -> /level_shifter3/DIR1
- S5 pad A1: /pin_header/DIR2_7 -> /level_shifter4/DIR2
- S5 pad B1: /pin_header/DIR1_7 -> /level_shifter4/DIR1
- S6 pad A1: /pin_header/DIR2_3 -> /level_shifter5/DIR2
- S6 pad B1: /pin_header/DIR1_3 -> /level_shifter5/DIR1
- S7 pad A1: /pin_header/DIR2_5 -> /level_shifter6/DIR2
- S7 pad B1: /pin_header/DIR1_5 -> /level_shifter6/DIR1
- U1 pad 2: /VCCD18 -> VCCD18
- U1 pad 4: /VCCD18 -> VCCD18
- U11 pad 1: /pin_header/DIR1_5 -> /level_shifter/DIR1
- U11 pad 11: /pin_header/OPD7 -> MC1_69
- U11 pad 12: /pin_header/OPD8 -> MC1_71
- U11 pad 13: /pin_header/OPD9 -> MC2_26
- U11 pad 14: /pin_header/OPD10 -> MC2_28
- U11 pad 16: /pin_header/OPD11 -> MC2_30
- U11 pad 17: /pin_header/OPD12 -> MC2_32
- U11 pad 18: V_Level_Shift -> VCCD33
- U11 pad 19: /pin_header/OPD13 -> MC2_34
- U11 pad 2: /pin_header/OPD1 -> MC1_57
- U11 pad 20: /pin_header/OPD14 -> MC2_38
- U11 pad 22: /pin_header/OPD15 -> MC2_40
- U11 pad 23: /pin_header/OPD16 -> MC2_42
- U11 pad 24: /pin_header/DIR2_5 -> /level_shifter/DIR2
- U11 pad 25: unconnected-(U11-*2OE-Pad25) -> Net-(U11-*2OE)
- U11 pad 26: /pin_header/OPF16 -> MC2_42_PIN
- U11 pad 27: /pin_header/OPF15 -> MC2_40_PIN
- U11 pad 29: /pin_header/OPF14 -> MC2_38_PIN
- U11 pad 3: /pin_header/OPD2 -> MC1_59
- U11 pad 30: /pin_header/OPF13 -> MC2_34_PIN
- U11 pad 32: /pin_header/OPF12 -> MC2_32_PIN
- U11 pad 33: /pin_header/OPF11 -> MC2_30_PIN
- U11 pad 35: /pin_header/OPF10 -> MC2_28_PIN
- U11 pad 36: /pin_header/OPF9 -> MC2_26_PIN
- U11 pad 37: /pin_header/OPF8 -> MC1_71_PIN
- U11 pad 38: /pin_header/OPF7 -> MC1_69_PIN
- U11 pad 40: /pin_header/OPF6 -> MC1_67_PIN
- U11 pad 41: /pin_header/OPF5 -> MC1_65_PIN
- U11 pad 43: /pin_header/OPF4 -> MC1_63_PIN
- U11 pad 44: /pin_header/OPF3 -> MC1_61_PIN
- U11 pad 46: /pin_header/OPF2 -> MC1_59_PIN
- U11 pad 47: /pin_header/OPF1 -> MC1_57_PIN
- U11 pad 48: unconnected-(U11-*1OE-Pad48) -> Net-(U11-*1OE)
- U11 pad 5: /pin_header/OPD3 -> MC1_61
- U11 pad 6: /pin_header/OPD4 -> MC1_63
- U11 pad 7: V_Level_Shift -> VCCD33
- U11 pad 8: /pin_header/OPD5 -> MC1_65
- U11 pad 9: /pin_header/OPD6 -> MC1_67
- U12 pad 1: /pin_header/DIR1_3 -> /level_shifter1/DIR1
- U12 pad 11: /pin_header/OPC7 -> MC2_58
- U12 pad 12: /pin_header/OPC8 -> MC2_60
- U12 pad 13: /pin_header/OPC9 -> MC2_62
- U12 pad 14: /pin_header/OPC10 -> MC2_64
- U12 pad 16: /pin_header/OPC11 -> MC2_66
- U12 pad 17: /pin_header/OPC12 -> MC2_68
- U12 pad 18: V_Level_Shift -> VCCD33
- U12 pad 19: /pin_header/OPC13 -> MC2_70
- U12 pad 2: /pin_header/OPC1 -> MC2_44
- U12 pad 20: /pin_header/OPC14 -> MC2_72
- U12 pad 22: /pin_header/OPC15 -> MC2_74
- U12 pad 23: /pin_header/OPC16 -> MC2_76
- U12 pad 24: /pin_header/DIR2_3 -> /level_shifter1/DIR2
- U12 pad 25: unconnected-(U12-*2OE-Pad25) -> Net-(U12-*2OE)
- U12 pad 26: /pin_header/OPE16 -> MC2_76_PIN
- U12 pad 27: /pin_header/OPE15 -> MC2_74_PIN
- U12 pad 29: /pin_header/OPE14 -> MC2_72_PIN
- U12 pad 3: /pin_header/OPC2 -> MC2_46
- U12 pad 30: /pin_header/OPE13 -> MC2_70_PIN
- U12 pad 32: /pin_header/OPE12 -> MC2_68_PIN
- U12 pad 33: /pin_header/OPE11 -> MC2_66_PIN
- U12 pad 35: /pin_header/OPE10 -> MC2_64_PIN
- U12 pad 36: /pin_header/OPE9 -> MC2_62_PIN
- U12 pad 37: /pin_header/OPE8 -> MC2_60_PIN
- U12 pad 38: /pin_header/OPE7 -> MC2_58_PIN
- U12 pad 40: /pin_header/OPE6 -> MC2_54_PIN
- U12 pad 41: /pin_header/OPE5 -> MC2_52_PIN
- U12 pad 43: /pin_header/OPE4 -> MC2_50_PIN
- U12 pad 44: /pin_header/OPE3 -> MC2_48_PIN
- U12 pad 46: /pin_header/OPE2 -> MC2_46_PIN
- U12 pad 47: /pin_header/OPE1 -> MC2_44_PIN
- U12 pad 48: unconnected-(U12-*1OE-Pad48) -> Net-(U12-*1OE)
- U12 pad 5: /pin_header/OPC3 -> MC2_48
- U12 pad 6: /pin_header/OPC4 -> MC2_50
- U12 pad 7: V_Level_Shift -> VCCD33
- U12 pad 8: /pin_header/OPC5 -> MC2_52
- U12 pad 9: /pin_header/OPC6 -> MC2_54
- U13 pad 1: /pin_header/DIR1_6 -> /level_shifter2/DIR1
- U13 pad 11: /pin_header/HF7 -> MC2_27
- U13 pad 12: /pin_header/HF8 -> MC2_29
- U13 pad 13: /pin_header/HF9 -> MC2_31
- U13 pad 14: /pin_header/HF10 -> MC2_33
- U13 pad 16: /pin_header/HF11 -> MC2_37
- U13 pad 17: /pin_header/HF12 -> MC2_39
- U13 pad 18: V_Level_Shift -> VCCD33
- U13 pad 19: /pin_header/HF13 -> MC2_41
- U13 pad 2: /pin_header/HF1 -> MC2_15
- U13 pad 20: /pin_header/HF14 -> MC2_43
- U13 pad 22: /pin_header/HF15 -> MC2_45
- U13 pad 23: /pin_header/HF16 -> MC2_10
- U13 pad 24: /pin_header/DIR2_6 -> /level_shifter2/DIR2
- U13 pad 25: unconnected-(U13-*2OE-Pad25) -> Net-(U13-*2OE)
- U13 pad 26: /pin_header/OPB16 -> MC2_10_PIN
- U13 pad 27: /pin_header/OPB15 -> MC2_45_PIN
- U13 pad 29: /pin_header/OPB14 -> MC2_43_PIN
- U13 pad 3: /pin_header/HF2 -> MC2_17
- U13 pad 30: /pin_header/OPB13 -> MC2_41_PIN
- U13 pad 32: /pin_header/OPB12 -> MC2_39_PIN
- U13 pad 33: /pin_header/OPB11 -> MC2_37_PIN
- U13 pad 35: /pin_header/OPB10 -> MC2_33_PIN
- U13 pad 36: /pin_header/OPB9 -> MC2_31_PIN
- U13 pad 37: /pin_header/OPB8 -> MC2_29_PIN
- U13 pad 38: /pin_header/OPB7 -> MC2_27_PIN
- U13 pad 40: /pin_header/OPB6 -> MC2_25_PIN
- U13 pad 41: /pin_header/OPB5 -> MC2_23_PIN
- U13 pad 43: /pin_header/OPB4 -> MC2_21_PIN
- U13 pad 44: /pin_header/OPB3 -> MC2_19_PIN
- U13 pad 46: /pin_header/OPB2 -> MC2_17_PIN
- U13 pad 47: /pin_header/OPB1 -> MC2_15_PIN
- U13 pad 48: unconnected-(U13-*1OE-Pad48) -> Net-(U13-*1OE)
- U13 pad 5: /pin_header/HF3 -> MC2_19
- U13 pad 6: /pin_header/HF4 -> MC2_21
- U13 pad 7: V_Level_Shift -> VCCD33
- U13 pad 8: /pin_header/HF5 -> MC2_23
- U13 pad 9: /pin_header/HF6 -> MC2_25
- U14 pad 1: /pin_header/DIR1_4 -> /level_shifter3/DIR1
- U14 pad 11: /pin_header/OPG7 -> MC2_61
- U14 pad 12: /pin_header/OPG8 -> MC2_63
- U14 pad 13: /pin_header/OPG9 -> MC2_65
- U14 pad 14: /pin_header/OPG10 -> MC2_67
- U14 pad 16: /pin_header/OPG11 -> MC2_69
- U14 pad 17: /pin_header/OPG12 -> MC2_71
- U14 pad 18: V_Level_Shift -> VCCD33
- U14 pad 19: /pin_header/OPG13 -> MC2_73
- U14 pad 2: /pin_header/OPG1 -> MC2_47
- U14 pad 20: /pin_header/OPG14 -> MC2_75
- U14 pad 22: /pin_header/OPG15 -> MC2_77
- U14 pad 23: /pin_header/OPG16 -> MC2_79
- U14 pad 24: /pin_header/DIR2_4 -> /level_shifter3/DIR2
- U14 pad 25: unconnected-(U14-*2OE-Pad25) -> Net-(U14-*2OE)
- U14 pad 26: /pin_header/HD16 -> MC2_79_PIN
- U14 pad 27: /pin_header/HD15 -> MC2_77_PIN
- U14 pad 29: /pin_header/HD14 -> MC2_75_PIN
- U14 pad 3: /pin_header/OPG2 -> MC2_49
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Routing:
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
